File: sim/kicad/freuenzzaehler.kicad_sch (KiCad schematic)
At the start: 36 parts, among them IC1 74HC4017, IC2 74HC74, IC3 74HC4060, IC4 4026, IC5 4026, IC6 4026, IC7 4026, IC8 4026, Q1 3.2768MHz, T1 SF245, U1 7805

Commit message: KiCad-Plan: echte Verdrahtung + Power-Symbole (erkennbarer Schaltplan)
- Segmentleitungen Zaehler->Anzeige und Carry-Kette als echte Draehte
- Power-Symbole (+5V/GND) statt Text, lesbare lokale Netz-Labels
- 4026-Symbol: Takt/Steuerung links, Versorgung+Segmente rechts
- Generator erzeugt zusaetzlich preview.png zur Layout-Kontrolle
- Validiert mit kiutils (13 Symbole, 88 Instanzen, 154 Draehte)
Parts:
- DISP1: value 7SEG St.1 -> 7SEG-1
- DISP2: value 7SEG St.2 -> 7SEG-2
- DISP3: value 7SEG St.3 -> 7SEG-3
- DISP4: value 7SEG St.4 -> 7SEG-4
- DISP5: value 7SEG St.5 -> 7SEG-5
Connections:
- net GND is gone; now on net +5V: C1.2, C10.2, C11.2, C12.2, C2.2, C6.2, C7.2, C8.2, C9.2, D1.1 (A), DISP1.8 (CC), DISP2.8 (CC), DISP3.8 (CC), DISP4.8 (CC), DISP5.8 (CC), IC1.13 (CKEN), IC1.15 (MR), IC1.8 (VSS), IC2.7 (GND), IC3.12 (MR), IC3.8 (VSS), IC4.8 (VSS), IC5.8 (VSS), IC6.8 (VSS), IC7.8 (VSS), IC8.8 (VSS), R3.2, R7.2, T1.3 (E), U1.2 (GND)
- net CAR1: no longer names the net of IC4.5 (CO), IC5.1 (CLK)
- net CAR2: no longer names the net of IC5.5 (CO), IC6.1 (CLK)
- net CAR3: no longer names the net of IC6.5 (CO), IC7.1 (CLK)
- net CAR4: no longer names the net of IC7.5 (CO), IC8.1 (CLK)
- net S1a: no longer names the net of DISP1.1 (a), IC4.10 (a)
- net S1b: no longer names the net of DISP1.2 (b), IC4.12 (b)
- net S1c: no longer names the net of DISP1.3 (c), IC4.13 (c)
- net S1d: no longer names the net of DISP1.4 (d), IC4.9 (d)
- net S1e: no longer names the net of DISP1.5 (e), IC4.11 (e)
- net S1f: no longer names the net of DISP1.6 (f), IC4.6 (f)
- net S1g: no longer names the net of DISP1.7 (g), IC4.7 (g)
- net S2a: no longer names the net of DISP2.1 (a), IC5.10 (a)
- net S2b: no longer names the net of DISP2.2 (b), IC5.12 (b)
- net S2c: no longer names the net of DISP2.3 (c), IC5.13 (c)
- net S2d: no longer names the net of DISP2.4 (d), IC5.9 (d)
- net S2e: no longer names the net of DISP2.5 (e), IC5.11 (e)
- net S2f: no longer names the net of DISP2.6 (f), IC5.6 (f)
- net S2g: no longer names the net of DISP2.7 (g), IC5.7 (g)
- net S3a: no longer names the net of DISP3.1 (a), IC6.10 (a)
- net S3b: no longer names the net of DISP3.2 (b), IC6.12 (b)
- net S3c: no longer names the net of DISP3.3 (c), IC6.13 (c)
- net S3d: no longer names the net of DISP3.4 (d), IC6.9 (d)
- net S3e: no longer names the net of DISP3.5 (e), IC6.11 (e)
- net S3f: no longer names the net of DISP3.6 (f), IC6.6 (f)
- net S3g: no longer names the net of DISP3.7 (g), IC6.7 (g)
- net S4a: no longer names the net of DISP4.1 (a), IC7.10 (a)
- net S4b: no longer names the net of DISP4.2 (b), IC7.12 (b)
- net S4c: no longer names the net of DISP4.3 (c), IC7.13 (c)
- net S4d: no longer names the net of DISP4.4 (d), IC7.9 (d)
- net S4e: no longer names the net of DISP4.5 (e), IC7.11 (e)
- net S4f: no longer names the net of DISP4.6 (f), IC7.6 (f)
- net S4g: no longer names the net of DISP4.7 (g), IC7.7 (g)
- net S5a: no longer names the net of DISP5.1 (a), IC8.10 (a)
- net S5b: no longer names the net of DISP5.2 (b), IC8.12 (b)
- net S5c: no longer names the net of DISP5.3 (c), IC8.13 (c)
- net S5d: no longer names the net of DISP5.4 (d), IC8.9 (d)
- net S5e: no longer names the net of DISP5.5 (e), IC8.11 (e)
- net S5f: no longer names the net of DISP5.6 (f), IC8.6 (f)
- net S5g: no longer names the net of DISP5.7 (g), IC8.7 (g)
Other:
- note added: "RESET-ERZEUGUNG (Teil 6)"
- note added: "UB = +Ub (DC-Buchse BU1, 7..20V)"
- note added: "ZAEHLERKETTE + ANZEIGE (Teil 3/4) - 5 Stellen, Carry-Kette + Segmentleitungen"
- note removed: "RESET (Teil 6)"
- note removed: "UB = +Ub (DC-Buchse BU1, 7...20V)"
- note removed: "ZAEHLERKETTE + ANZEIGE (Teil 3/4)"
- company: Tutorial-Projekt FreuenzZaehler -> Tutorial FreuenzZaehler

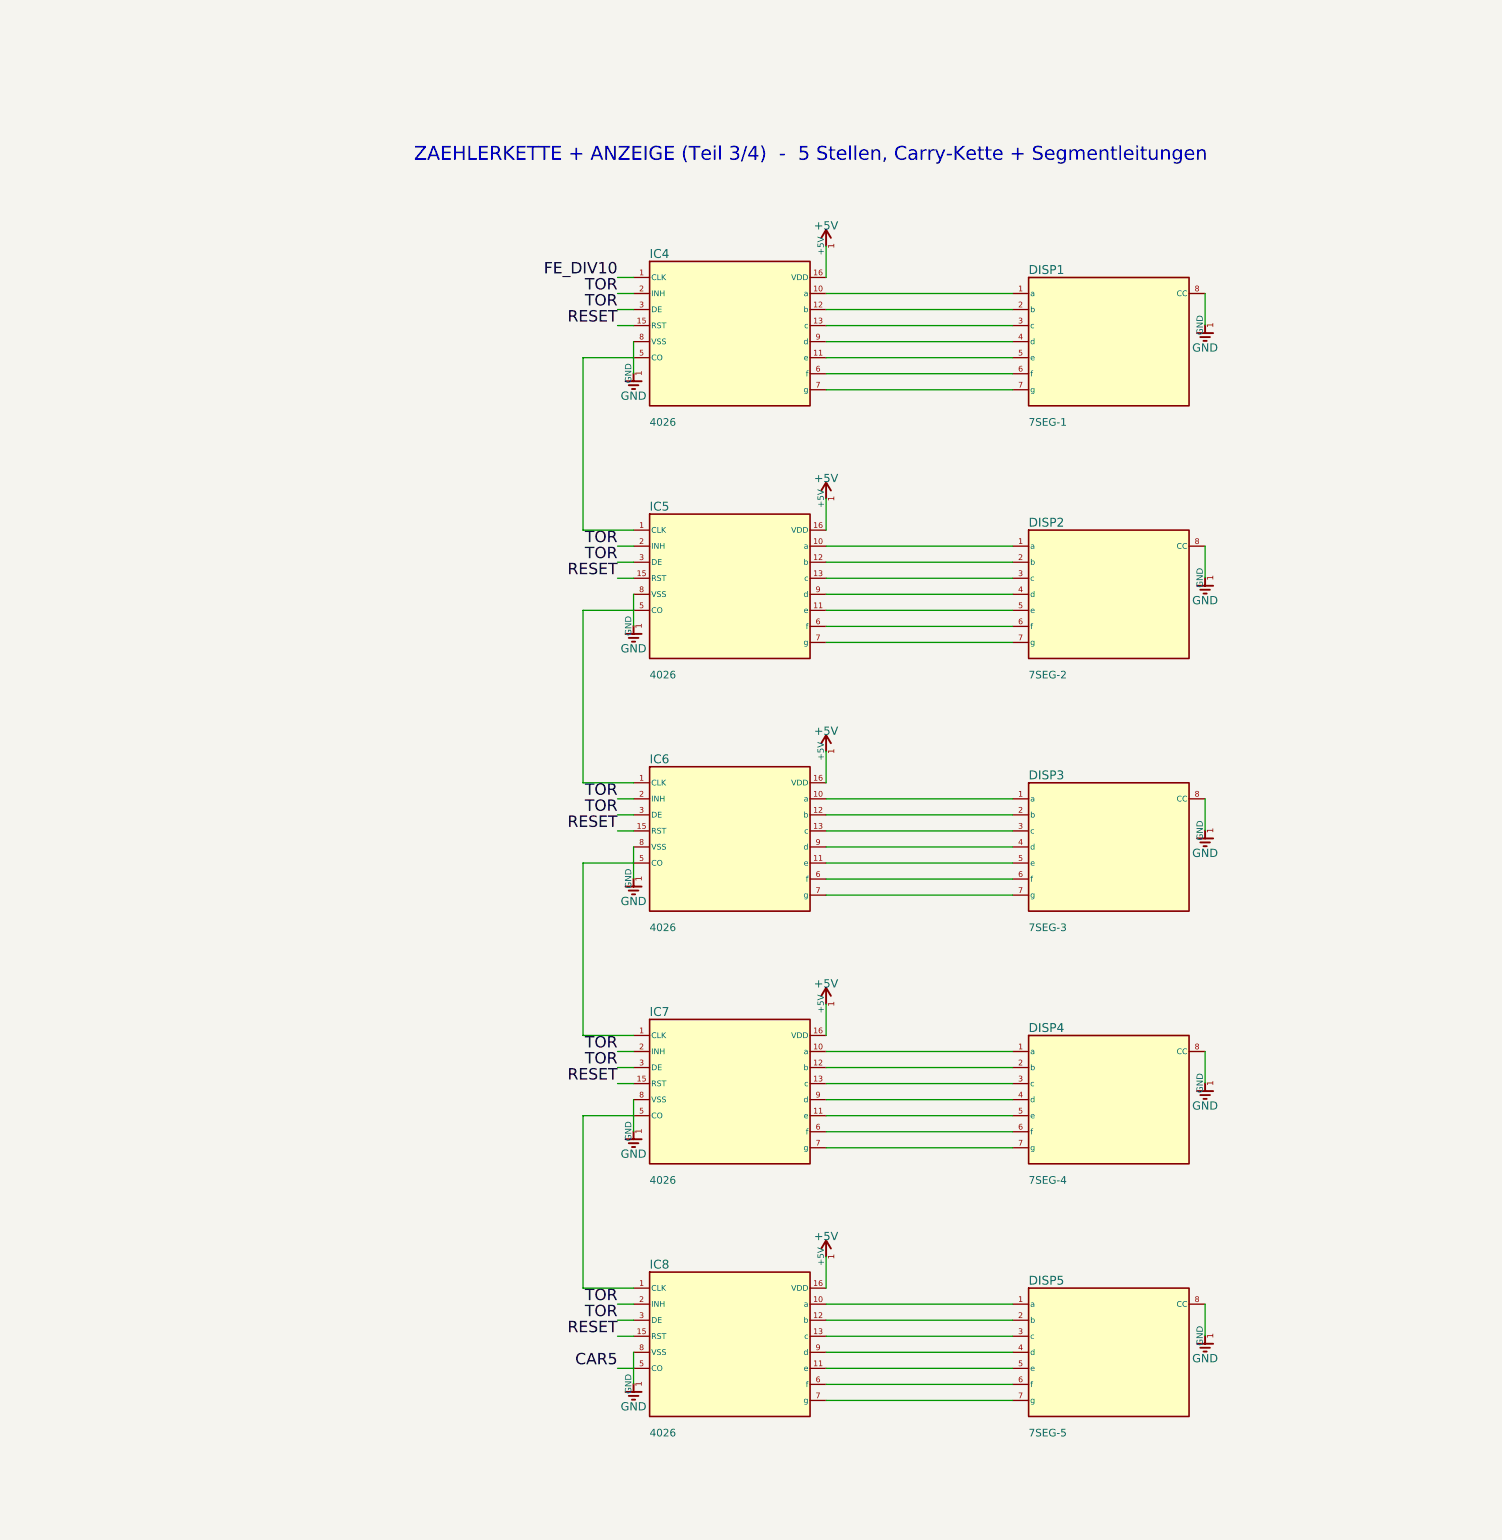
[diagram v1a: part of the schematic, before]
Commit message: KiCad: vollstaendiges Projekt (.kicad_pro) + aufgeraeumtes Layout
- freuenzzaehler.kicad_pro ergaenzt -> oeffnet ueber Projekt-Manager
  (behebt Fehler 'Endung stimmt nicht')
- Layout kompakter: Zaehlerkette naeher herangerueckt, Luecke geschlossen
- README: Anleitung zum Oeffnen in KiCad-Desktop (Projekt oeffnen)
- Validiert: kicad_sch (kiutils) + kicad_pro (JSON)
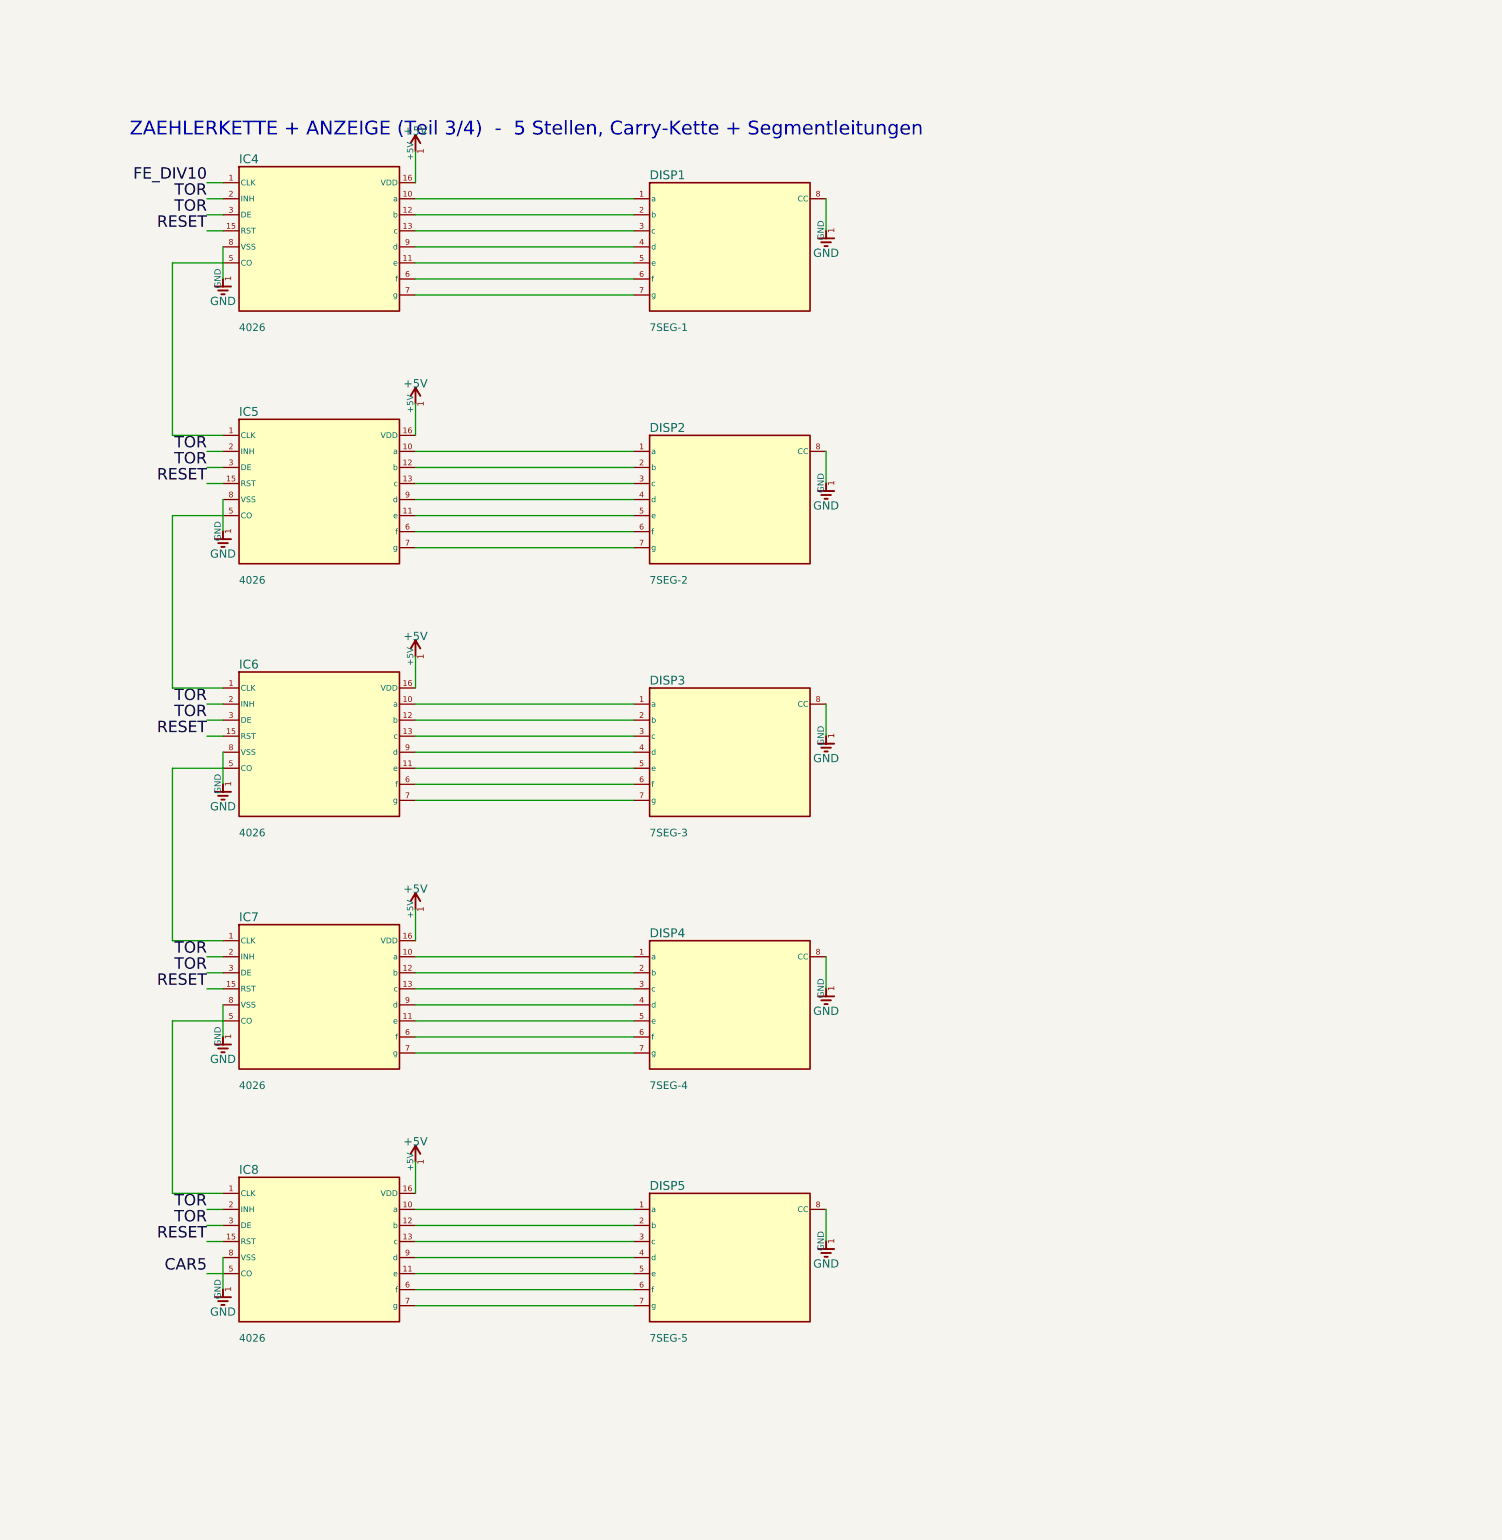
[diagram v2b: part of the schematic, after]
